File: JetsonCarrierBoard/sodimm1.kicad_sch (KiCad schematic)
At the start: 1 part

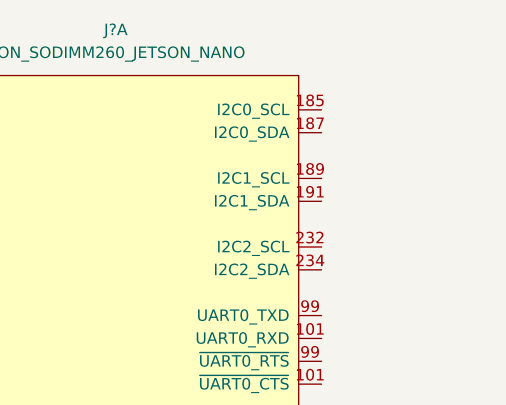
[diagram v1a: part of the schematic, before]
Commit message: Finished USB-C w/ Alt mode and PD Wiring V1
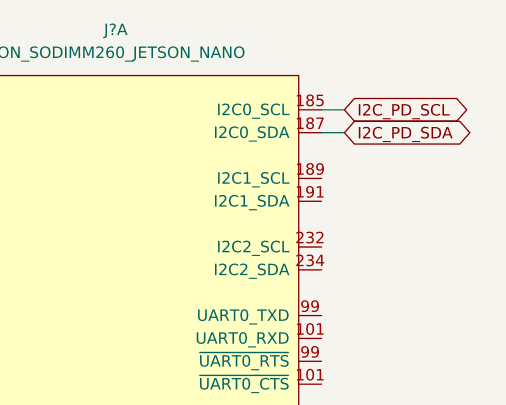
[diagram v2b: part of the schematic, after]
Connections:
- net I2C_PD_SCL: now reaches J?.185 (I2C0_SCL)
- net I2C_PD_SDA: now reaches J?.187 (I2C0_SDA)
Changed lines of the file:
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@@
+    (stroke (width 0) (type default) (color 0 0 0 0))
+  )
+  (wire (pts (xy 130.81 29.21) (xy 133.35 29.21))
     (stroke (width 0) (type default) (color 0 0 0 0))
   )
@@
   )
   (wire (pts (xy 82.55 29.21) (xy 82.55 31.75))
+    (stroke (width 0) (type default) (color 0 0 0 0))
+  )
+  (wire (pts (xy 130.81 31.75) (xy 133.35 31.75))
     (stroke (width 0) (type default) (color 0 0 0 0))
   )
@@
     (stroke (width 0) (type default) (color 0 0 0 0))
   )
+  (global_label "I2C_PD_SDA" (shape bidirectional) (at 133.35 31.75 0) (fields_autoplaced)
+    (effects (font (size 1.27 1.27)) (justify left))
+    (property "Intersheet References" "${INTERSHEET_REFS}" (id 0) (at 146.8907 31.6706 0)
+      (effects (font (size 1.27 1.27)) (justify left) hide)
+    )
+  )
+  (global_label "I2C_PD_SCL" (shape bidirectional) (at 133.35 29.21 0) (fields_autoplaced)
+    (effects (font (size 1.27 1.27)) (justify left))
+    (property "Intersheet References" "${INTERSHEET_REFS}" (id 0) (at 146.8302 29.1306 0)
+      (effects (font (size 1.27 1.27)) (justify left) hide)
+    )
+  )
   (symbol (lib_id "power:GND") (at 82.55 173.99 0) (unit 1)

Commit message: Small changes
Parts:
- added C?: 560u, symbol Device:C_Polarized
- added C? (x2): 100u, symbol Device:C
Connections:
- net +5V: now also C?.1, C?.1, C?.1
- net GND: now also C?.2, C?.2, C?.2
- net ELRS_TX: now reaches J?.101 (~{UART0_CTS})
- net ELRS_RX: now reaches J?.99 (~{UART0_RTS})
- no-connect marks 2 -> 7
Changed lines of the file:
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@@
   (junction (at 82.55 135.89) (diameter 0) (color 0 0 0 0)
   )
+  (junction (at 59.69 36.83) (diameter 0) (color 0 0 0 0)
+  )
   (junction (at 82.55 29.21) (diameter 0) (color 0 0 0 0)
   )
+  (junction (at 46.99 36.83) (diameter 0) (color 0 0 0 0)
+  )
   (junction (at 82.55 92.71) (diameter 0) (color 0 0 0 0)
   )
   (junction (at 82.55 90.17) (diameter 0) (color 0 0 0 0)
   )
+  (junction (at 72.39 29.21) (diameter 0) (color 0 0 0 0)
+  )
+  (junction (at 59.69 29.21) (diameter 0) (color 0 0 0 0)
+  )
   (junction (at 82.55 87.63) (diameter 0) (color 0 0 0 0)
   )
@@
   (junction (at 82.55 46.99) (diameter 0) (color 0 0 0 0)
   )
+  (junction (at 46.99 29.21) (diameter 0) (color 0 0 0 0)
+  )
   (junction (at 133.35 166.37) (diameter 0) (color 0 0 0 0)
   )
@@
   (junction (at 133.35 125.73) (diameter 0) (color 0 0 0 0)
   )
+  (no_connect (at 130.81 101.6))
+  (no_connect (at 130.81 72.39))
+  (no_connect (at 130.81 69.85))
+  (no_connect (at 130.81 59.69))
+  (no_connect (at 130.81 57.15))
   (no_connect (at 130.81 88.9))
   (no_connect (at 130.81 86.36))
@@
     (stroke (width 0) (type default) (color 0 0 0 0))
   )
+  (wire (pts (xy 59.69 36.83) (xy 72.39 36.83))
+    (stroke (width 0) (type default) (color 0 0 0 0))
+  )
   (wire (pts (xy 85.09 57.15) (xy 82.55 57.15))
     (stroke (width 0) (type default) (color 0 0 0 0))
@@
     (stroke (width 0) (type default) (color 0 0 0 0))
   )
+  (wire (pts (xy 46.99 29.21) (xy 59.69 29.21))
+    (stroke (width 0) (type default) (color 0 0 0 0))
+  )
   (wire (pts (xy 82.55 97.79) (xy 82.55 100.33))
     (stroke (width 0) (type default) (color 0 0 0 0))
@@
     (stroke (width 0) (type default) (color 0 0 0 0))
   )
+  (wire (pts (xy 46.99 36.83) (xy 46.99 39.37))
+    (stroke (width 0) (type default) (color 0 0 0 0))
+  )
+  (wire (pts (xy 130.81 52.07) (xy 134.62 52.07))
+    (stroke (width 0) (type default) (color 0 0 0 0))
+  )
   (wire (pts (xy 82.55 41.91) (xy 85.09 41.91))
     (stroke (width 0) (type default) (color 0 0 0 0))
@@
     (stroke (width 0) (type default) (color 0 0 0 0))
   )
-  (wire (pts (xy 82.55 26.67) (xy 82.55 29.21))
-    (stroke (width 0) (type default) (color 0 0 0 0))
-  )
   (wire (pts (xy 82.55 64.77) (xy 85.09 64.77))
     (stroke (width 0) (type default) (color 0 0 0 0))
@@
     (stroke (width 0) (type default) (color 0 0 0 0))
   )
+  (wire (pts (xy 130.81 54.61) (xy 134.62 54.61))
+    (stroke (width 0) (type default) (color 0 0 0 0))
+  )
   (wire (pts (xy 82.55 166.37) (xy 85.09 166.37))
     (stroke (width 0) (type default) (color 0 0 0 0))
   )
+  (wire (pts (xy 46.99 26.67) (xy 46.99 29.21))
+    (stroke (width 0) (type default) (color 0 0 0 0))
+  )
   (wire (pts (xy 82.55 57.15) (xy 82.55 59.69))
     (stroke (width 0) (type default) (color 0 0 0 0))
@@
     (stroke (width 0) (type default) (color 0 0 0 0))
   )
+  (wire (pts (xy 72.39 29.21) (xy 82.55 29.21))
+    (stroke (width 0) (type default) (color 0 0 0 0))
+  )
   (wire (pts (xy 82.55 135.89) (xy 85.09 135.89))
     (stroke (width 0) (type default) (color 0 0 0 0))
   )
+  (wire (pts (xy 59.69 29.21) (xy 72.39 29.21))
+    (stroke (width 0) (type default) (color 0 0 0 0))
+  )
   (wire (pts (xy 133.35 120.65) (xy 133.35 123.19))
     (stroke (width 0) (type default) (color 0 0 0 0))
@@
   )
   (wire (pts (xy 82.55 163.83) (xy 85.09 163.83))
+    (stroke (width 0) (type default) (color 0 0 0 0))
+  )
+  (wire (pts (xy 46.99 36.83) (xy 59.69 36.83))
     (stroke (width 0) (type default) (color 0 0 0 0))
   )
@@
     (effects (font (size 1.27 1.27)) (justify left))
     (property "Intersheet References" "${INTERSHEET_REFS}" (id 0) (at 146.8302 29.1306 0)
+      (effects (font (size 1.27 1.27)) (justify left) hide)
+    )
+  )
+  (global_label "ELRS_RX" (shape input) (at 134.62 52.07 0) (fields_autoplaced)
+    (effects (font (size 1.27 1.27)) (justify left))
+    (property "Intersheet References" "${INTERSHEET_REFS}" (id 0) (at 145.1369 51.9906 0)
+      (effects (font (size 1.27 1.27)) (justify left) hide)
+    )
+  )
+  (global_label "ELRS_TX" (shape input) (at 134.62 54.61 0) (fields_autoplaced)
+    (effects (font (size 1.27 1.27)) (justify left))
+    (property "Intersheet References" "${INTERSHEET_REFS}" (id 0) (at 144.8345 54.5306 0)
       (effects (font (size 1.27 1.27)) (justify left) hide)
     )
@@
     (pin "98")
   )
+  (symbol (lib_id "power:GND") (at 46.99 39.37 0) (unit 1)
+    (in_bom yes) (on_board yes)
+    (property "Reference" "#PWR?" (id 0) (at 46.99 45.72 0)
+      (effects (font (size 1.27 1.27)) hide)
+    )
+    (property "Value" "GND" (id 1) (at 46.99 43.18 0))
+    (property "Footprint" "" (id 2) (at 46.99 39.37 0)
+      (effects (font (size 1.27 1.27)) hide)
+    )
+    (property "Datasheet" "" (id 3) (at 46.99 39.37 0)
+      (effects (font (size 1.27 1.27)) hide)
+    )
+    (pin "1")
+  )
+  (symbol (lib_id "Device:C_Polarized") (at 46.99 33.02 0) (unit 1)
+    (in_bom yes) (on_board yes) (fields_autoplaced)
+    (property "Reference" "C?" (id 0) (at 50.8 30.8609 0)
+      (effects (font (size 1.27 1.27)) (justify left))
+    )
+    (property "Value" "560u" (id 1) (at 50.8 33.4009 0)
+      (effects (font (size 1.27 1.27)) (justify left))
+    )
+    (property "Footprint" "" (id 2) (at 47.9552 36.83 0)
+      (effects (font (size 1.27 1.27)) hide)
+    )
+    (property "Datasheet" "~" (id 3) (at 46.99 33.02 0)
+      (effects (font (size 1.27 1.27)) hide)
+    )
+    (pin "1")
+    (pin "2")
+  )
+  (symbol (lib_id "Device:C") (at 59.69 33.02 0) (unit 1)
+    (in_bom yes) (on_board yes) (fields_autoplaced)
+    (property "Reference" "C?" (id 0) (at 63.5 31.7499 0)
+      (effects (font (size 1.27 1.27)) (justify left))
+    )
+    (property "Value" "100u" (id 1) (at 63.5 34.2899 0)
+      (effects (font (size 1.27 1.27)) (justify left))
+    )
+    (property "Footprint" "" (id 2) (at 60.6552 36.83 0)
+      (effects (font (size 1.27 1.27)) hide)
+    )
+    (property "Datasheet" "~" (id 3) (at 59.69 33.02 0)
+      (effects (font (size 1.27 1.27)) hide)
+    )
+    (pin "1")
+    (pin "2")
+  )
   (symbol (lib_id "power:GND") (at 133.35 173.99 0) (unit 1)
     (in_bom yes) (on_board yes)
@@
     (pin "1")
   )
-  (symbol (lib_id "power:+5V") (at 82.55 26.67 0) (unit 1)
+  (symbol (lib_id "Device:C") (at 72.39 33.02 0) (unit 1)
     (in_bom yes) (on_board yes) (fields_autoplaced)
-    (property "Reference" "#PWR?" (id 0) (at 82.55 30.48 0)
-      (effects (font (size 1.27 1.27)) hide)
-    )
-    (property "Value" "+5V" (id 1) (at 82.55 21.59 0))
-    (property "Footprint" "" (id 2) (at 82.55 26.67 0)
-      (effects (font (size 1.27 1.27)) hide)
-    )
-    (property "Datasheet" "" (id 3) (at 82.55 26.67 0)
-      (effects (font (size 1.27 1.27)) hide)
-    )
+    (property "Reference" "C?" (id 0) (at 76.2 31.7499 0)
+      (effects (font (size 1.27 1.27)) (justify left))
+    )
+    (property "Value" "100u" (id 1) (at 76.2 34.2899 0)
+      (effects (font (size 1.27 1.27)) (justify left))
+    )
+    (property "Footprint" "" (id 2) (at 73.3552 36.83 0)
+      (effects (font (size 1.27 1.27)) hide)
+    )
+    (property "Datasheet" "~" (id 3) (at 72.39 33.02 0)
+      (effects (font (size 1.27 1.27)) hide)
+    )
+    (pin "1")
+    (pin "2")
+  )
+  (symbol (lib_id "power:+5V") (at 46.99 26.67 0) (unit 1)
+    (in_bom yes) (on_board yes) (fields_autoplaced)
+    (property "Reference" "#PWR?" (id 0) (at 46.99 30.48 0)
+      (effects (font (size 1.27 1.27)) hide)
+    )
+    (property "Value" "+5V" (id 1) (at 46.99 21.59 0))
+    (property "Footprint" "" (id 2) (at 46.99 26.67 0)
+      (effects (font (size 1.27 1.27)) hide)
+    )
+    (property "Datasheet" "" (id 3) (at 46.99 26.67 0)
+      (effects (font (size 1.27 1.27)) hide)
+    )

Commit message: Connections
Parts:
- added D? (x2): D_TVS, symbol Device:D_TVS
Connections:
- net GND: now also D?.1 (A1), D?.1 (A1)
- net I2C1_SCL: now reaches J?.189 (I2C1_SCL)
- net I2C1_SDA: now reaches J?.191 (I2C1_SDA)
- net UART1_TXD: now reaches J?.203 (UART1_TXD)
- net UART1_RXD: now reaches J?.205 (UART1_RXD)
- net FORCE_RECOVERY*: now reaches J?.214 (~{FORCE_RECOVERY})
- net FORCE_RECOVERY*: now also D?.2 (A2)
- net I2C2_SCL: now reaches J?.232 (I2C2_SCL)
- net SHUTDOWN_REQ*: now reaches J?.233 (~{SHUTDOWN_REQ})
- net I2C2_SDA: now reaches J?.234 (I2C2_SDA)
- net UART2_TXD: now reaches J?.236 ((DEBUG)_UART2_TXD)
- net POWER_EN: now reaches J?.237 (POWER_EN)
- net UART2_RXD: now reaches J?.238 ((DEBUG)_UART2_RXD)
- net SYS_RST*: now reaches J?.239 (~{SYS_RESET})
- net SYS_RST*: now also D?.2 (A2)
- no-connect marks 7 -> 9
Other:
- moved on the sheet: C?, J?A
